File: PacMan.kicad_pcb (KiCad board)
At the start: 2 copper layers, 139.7 x 114.3 mm, 165 parts, among them J1 POWER+, J10 SEG2 CellMen, J11 BAL1, J12 BAL2, J13 AIR Left, J14 AIR Right, J15 SEG1, J16 SEG2, J2 POWER-, J3 TSV IN, J4 Charge Detection, J5 SEG1 CellMen, J6 BusBar Current Sensor, J7 Panel, J8 SLOOP, J9 GLV/CAN, K1 G5Q-1A4 DC24, K2 T9AS1D12-24, K3 T9AS1D12-24, Q1 DMN3730U, Q2 DMN3730U, Q4 DMP10H4D2S, Q5 DMP10H4D2S, U1 MCP9804, U10 LTC4151, U11 INA592, U12 MEF1S2405SP3C, U13 V7805-500, U14 Si8600AC, U15 Si8600AC, U16 TEC3-2419, U17 TEC3-2419, U18 AP2204K-5.0, U19 INA233, U2 TEC2-4815WI, U20 INA233, U21 Si8600AC, U22 AP2204K-5.0, U3 ADM6320, U4 MCP2551-I-SN, U5 ESP32_DEVKITC, U6 MCP23008, U7 BQ32002, U8 ACHS-7122, U9 PDQE10-Q48-S24-D, Y1 RTC_32K

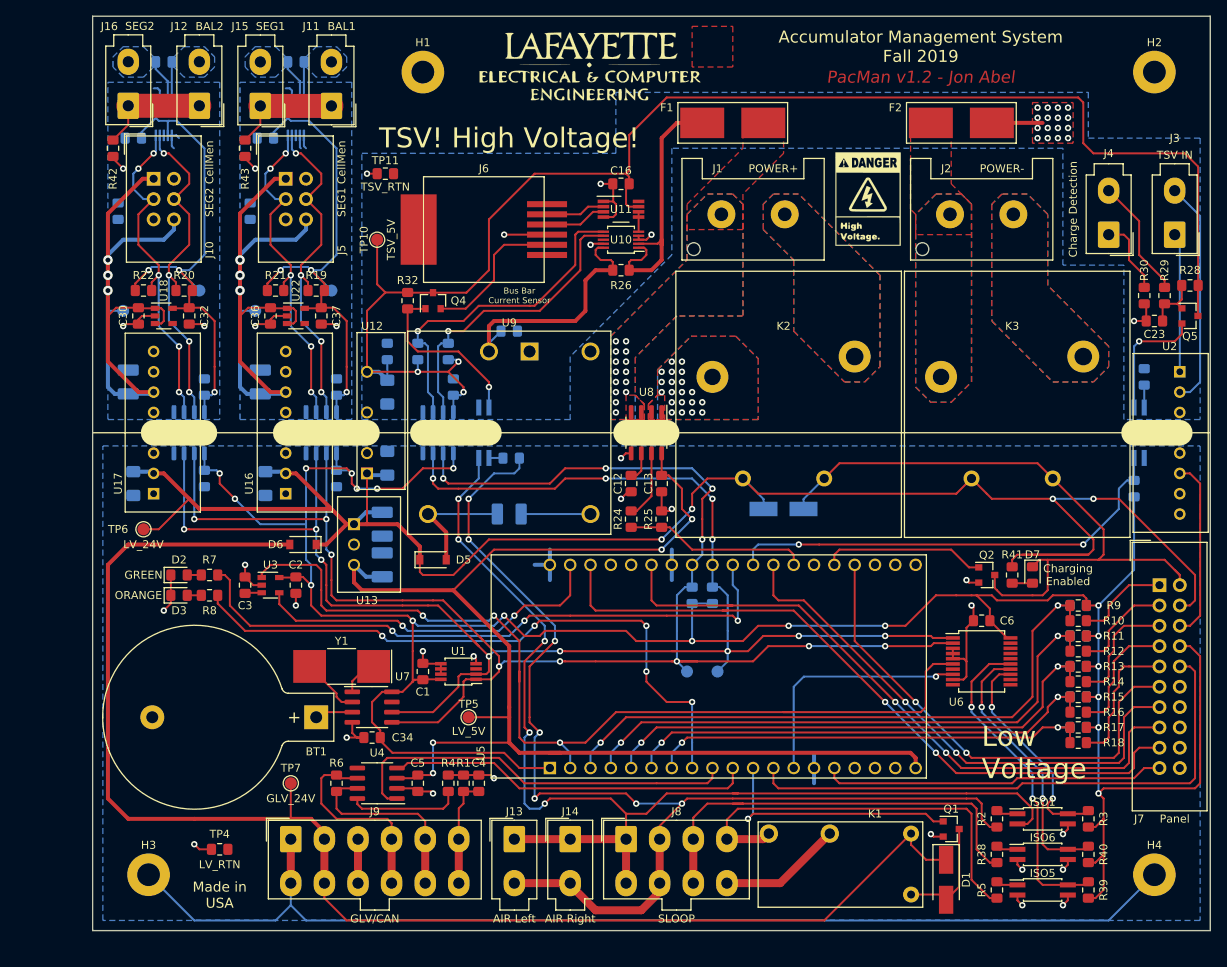
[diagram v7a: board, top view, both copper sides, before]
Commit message: completed reroute
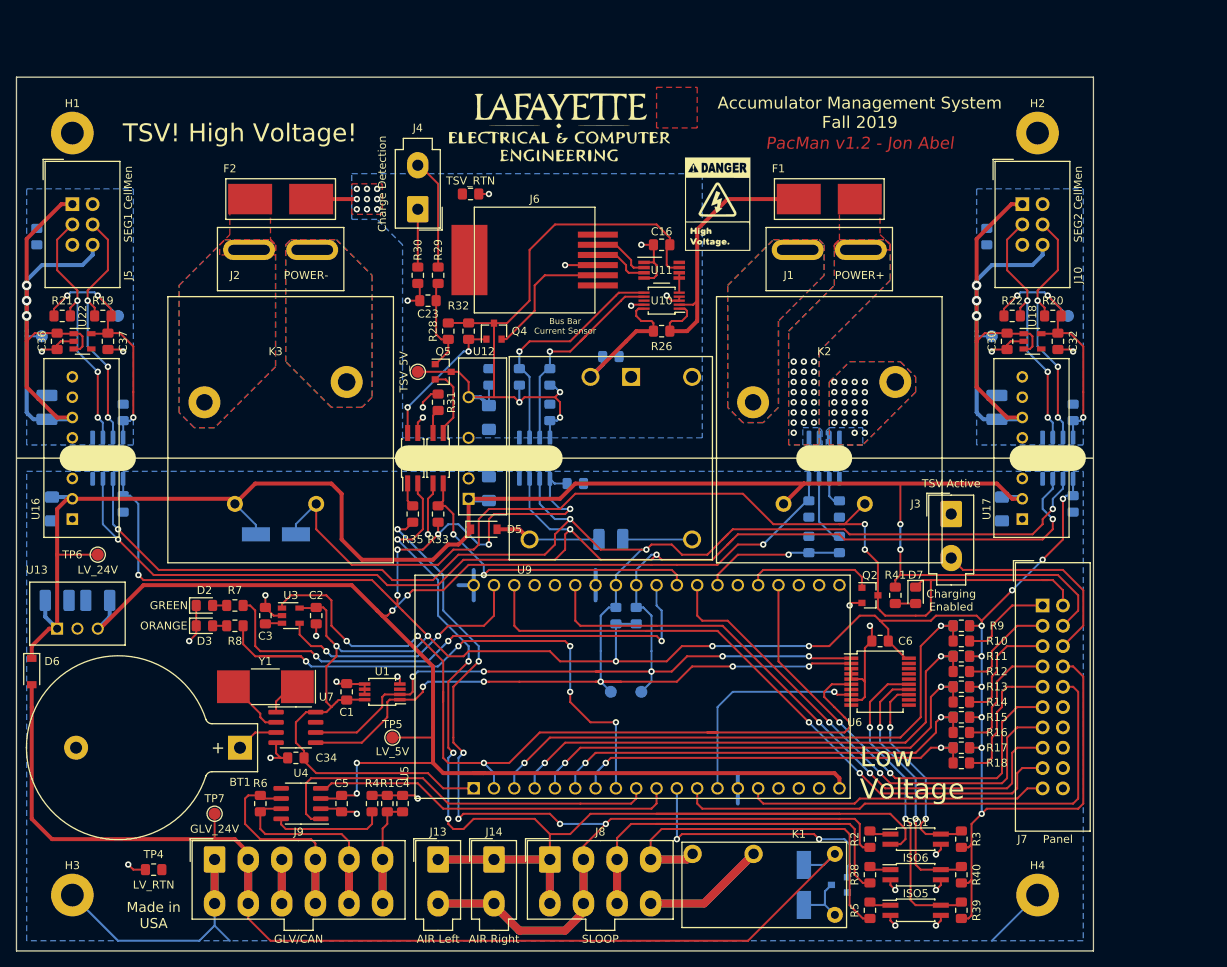
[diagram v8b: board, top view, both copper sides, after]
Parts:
- removed C33: 0.1u/50V, Capacitor_SMD:C_0805_2012Metric_Pad1.15x1.40mm_HandSolder
- removed G***: LOGO, Lafayette_Electric_Car_Footprints:pacman_github_link
- removed J11: BAL1, Lafayette_Electric_Car_Footprints:Molex_Mini-Fit_Jr_5566-02A_2x01_P4.20mm_Vertical
- removed J12: BAL2, Lafayette_Electric_Car_Footprints:Molex_Mini-Fit_Jr_5566-02A_2x01_P4.20mm_Vertical
- removed J15: SEG1, Lafayette_Electric_Car_Footprints:Molex_Mini-Fit_Jr_5566-02A_2x01_P4.20mm_Vertical
- removed J16: SEG2, Lafayette_Electric_Car_Footprints:Molex_Mini-Fit_Jr_5566-02A_2x01_P4.20mm_Vertical
- removed R36, R37: R, Resistor_SMD:R_0805_2012Metric_Pad1.15x1.40mm_HandSolder
- removed R42, R43: 10k, Resistor_SMD:R_0805_2012Metric_Pad1.15x1.40mm_HandSolder
- removed U19, U20: INA233, Package_SO:VSSOP-10_3x3mm_P0.5mm
- removed U2: TEC2-4815WI, Lafayette_Electric_Car_Footprints:TEC2-4815
- C12, C13, D1, Q1, R24, R25, U8: moved to B.Cu
- H1, H2, H3, H4: value MountingHole_Pad -> MountingHole_Pad_#4
- ISO2, ISO4, R31, R33, R35: moved to F.Cu
- J1, J2: footprint Lafayette_Electric_Car_Footprints:DF22-2P-7.92 -> Lafayette_Electric_Car_Footprints:Powerpole_PP45_FP_1x2
- J3: value TSV IN -> TSV Active
- moved C20 108.6 mm to (208.3, 86.4)
- moved C21 108.6 mm to (208.3, 97.8)
- moved C30 108.6 mm to (200.0, 77.5)
- moved J10 108.6 mm to (201.9, 60.3)
- moved R20 108.6 mm to (205.7, 74.3)
- moved TP12 108.6 mm to (198.1, 76.8)
- moved TP13 108.6 mm to (207.6, 74.3)
- moved TP14 108.6 mm to (197.5, 64.4)
- moved U17 108.6 mm to (201.9, 99.7)
- moved C29 108.6 mm to (198.8, 85.7)
- moved C32 108.6 mm to (206.4, 77.5)
- moved R22 108.6 mm to (200.7, 74.3)
- moved U15 108.6 mm to (206.4, 92.1)
- moved U18 108.6 mm to (203.2, 77.5)
- moved C26 108.6 mm to (199.4, 98.4)
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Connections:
- C31 pad 1: /SEG1_RTN -> /LV_3V3
- C31 pad 2: /SEG1_5V -> /GLV_RTN
- J1 pad 1: /CHRG_IN+ -> /PACK+
- J1 pad 2: /PACK+ -> /CHRG_IN+
- J3 pad 1: /TSV_VEHICLE- -> /GLV_RTN
- J3 pad 2: /TSV_VEHICLE+ -> /TSV_LIVE
- K2 pad 3: /Charging/CurrentSensor+ -> /CHRG_IN+
- K2 pad 4: /CHRG_IN+ -> /Charging/CurrentSensor+
- U8 pad 1: /Charging/CurrentSensor+ -> /PACK+
- U8 pad 2: /Charging/CurrentSensor+ -> /PACK+
- U8 pad 3: /PACK+ -> /Charging/CurrentSensor+
- U8 pad 4: /PACK+ -> /Charging/CurrentSensor+
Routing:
- net /TSV_5V: track 194.2 -> 88.4 mm
- net /CHS_GND: track 140.3 -> 45.5 mm
- net /CHRG_LED: track 82.5 -> 133.9 mm, vias 0 -> 2
- net /LV_5V: track 162.3 -> 203.9 mm, vias 4 -> 5
- net /SCL_GLV: track 209.6 -> 247.9 mm, vias 12 -> 9
- net /AIRS-: track 143.9 -> 179.5 mm, vias 5 -> 4
- net /GLV_24V: track 180.0 -> 145.9 mm
- net /SDA_GLV: track 212.5 -> 245.8 mm, vias 12 -> 9
- net /SEG2_5V: track 67.2 -> 34.9 mm
- net /SEG1_5V: track 65.3 -> 34.9 mm
- net /TSV_VEHICLE+: track 28.9 -> 0.00 mm
- net /LV_3V3: track 329.6 -> 356.1 mm, vias 19 -> 20
- net /SLOOP2: track 54.2 -> 75.3 mm
- net /TSV_VEHICLE-: track 17.4 -> 0.00 mm
- net /~CHRG_DETECT: track 57.4 -> 40.5 mm
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- removed copper zone on B.Cu, net /BAL_SEG1+
- removed copper zone on B.Cu, net /BAL_SEG2+
- removed copper zone on B.Cu, net /SEG1+
- removed copper zone on B.Cu, net /SEG2+
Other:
- board size 139.7 x 114.3 mm -> 134.6 x 109.2 mm
- board text removed: "Link to GitHub repository"
